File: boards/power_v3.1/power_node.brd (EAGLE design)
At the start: 80 x 51 mm, 31 parts, among them J1 AVR_SPI_PRG_6NS, J2 12146734, U1 ATtiny167, U2 MCP2025, U3 MC17XSF500

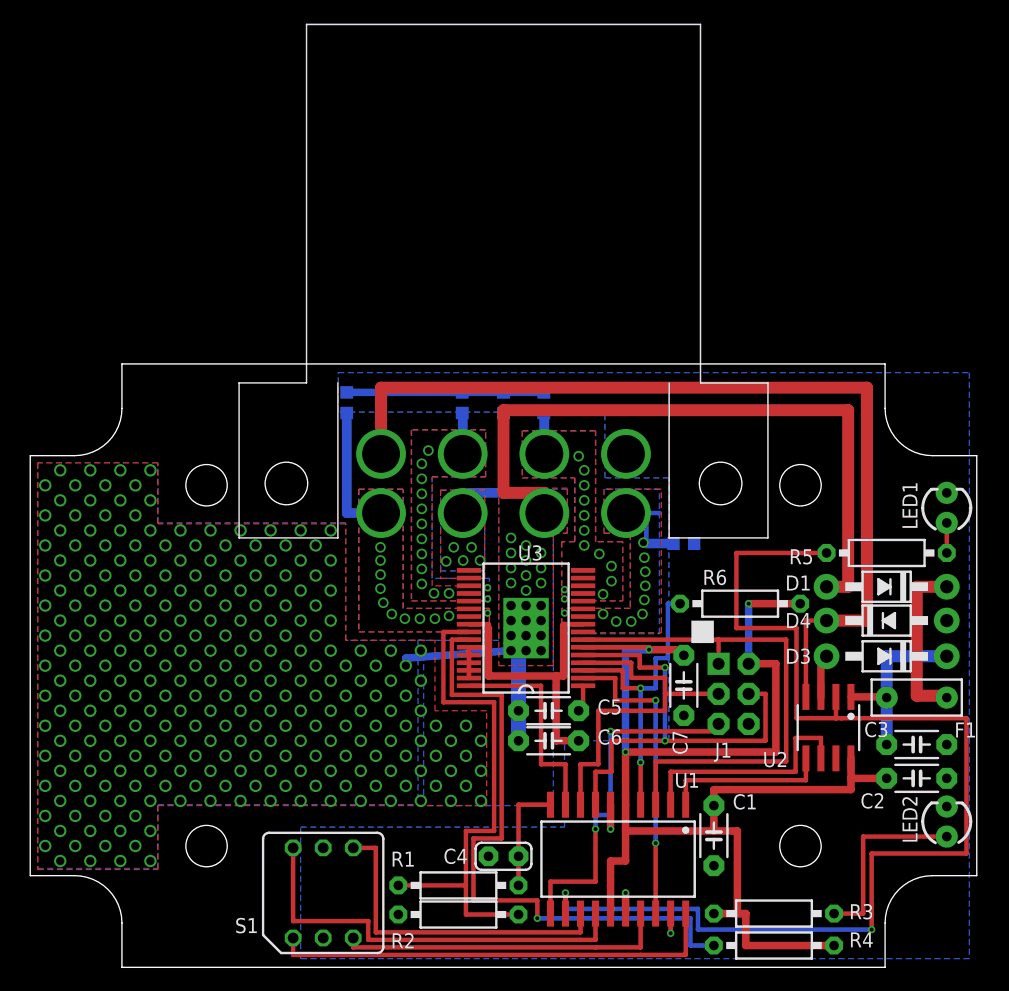
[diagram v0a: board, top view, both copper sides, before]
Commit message: Spin the power_v3 board, add more support code for it
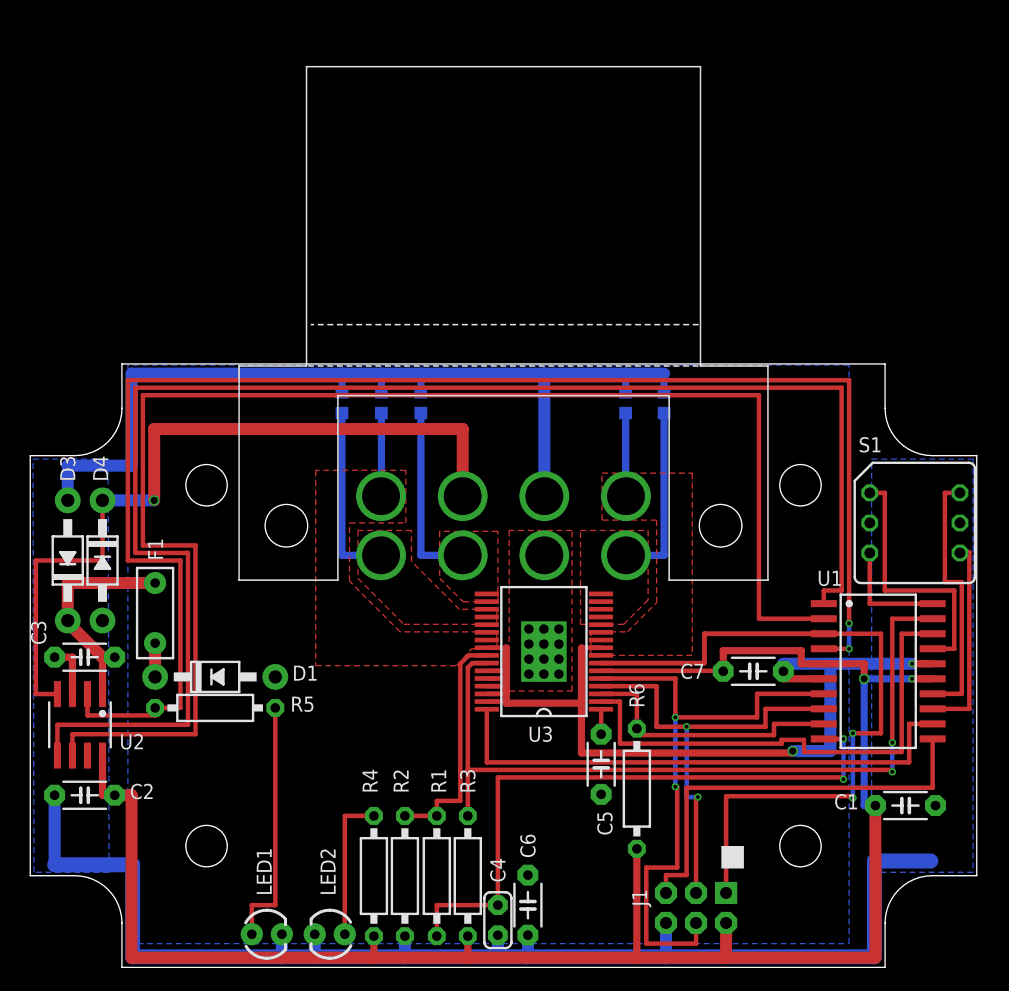
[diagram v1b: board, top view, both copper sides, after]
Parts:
- moved C3 70.7 mm to (12.2, 36.9), turned to 180 degrees
- moved C2 70.3 mm to (12.2, 25.2), turned to 180 degrees
- moved D3 69.7 mm to (10.8, 45.1), turned to 90 degrees
- moved LED1 67.8 mm to (27.6, 13.5), turned to 0 degrees
- moved D4 66.5 mm to (13.7, 45.1), turned to 270 degrees
- moved F1 64.8 mm to (18.2, 40.6), turned to 270 degrees
- moved U2 63.3 mm to (11.8, 31.2)
- moved S1 59.0 mm to (82.4, 48.3), turned to 180 degrees
- moved R5 58.2 mm to (23.3, 32.6)
- moved D1 57.3 mm to (23.3, 35.2), turned to 0 degrees
- moved LED2 53.0 mm to (32.9, 13.5), turned to 180 degrees
- moved R4 34.0 mm to (36.7, 18.4), turned to 270 degrees
- moved U1 27.1 mm to (79.3, 35.7), turned to 270 degrees
- moved R3 26.5 mm to (44.6, 18.4), turned to 270 degrees
- moved J1 18.4 mm to (63.9, 15.7), turned to 180 degrees
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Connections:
- net GND: now also J2.C; no longer J2.D
- net ID1: now also U1.17; no longer U1.20
- net ID4: now also U1.20; no longer U1.17
- net LIN: now also J2.B; no longer J2.A
- net LINCS: now also U1.4; no longer U1.12
- net OUT1: now also J2.A; no longer J2.H
- net OUT2: now also J2.D; no longer J2.E
- net OUT3: now also J2.H; no longer J2.B
- net OUT4: now also J2.E; no longer J2.C
- net SWCLK: now also U1.12; no longer U1.9
- net SWCS: now also U1.9; no longer U1.4
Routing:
- net GND: track 54.7 -> 269.6 mm
- net LINRX: track 14.1 -> 126.0 mm
- net LINTX: track 20.1 -> 121.7 mm
- net +12V: track 75.8 -> 0.00 mm, vias 278 -> 0
- net CSNS: track 9.52 -> 53.0 mm, vias 0 -> 2
- net +5V: track 117.4 -> 154.9 mm, vias 3 -> 2
- net LINCS: track 99.4 -> 128.2 mm
- net SWCLK: track 18.2 -> 45.4 mm
- net N$6: track 42.9 -> 20.1 mm
- net N$3: track 2.54 -> 21.1 mm
- net ID4: track 27.9 -> 9.60 mm
- net MISO: track 44.2 -> 61.5 mm, vias 0 -> 2
- net SWRSTB: track 26.0 -> 42.9 mm, vias 2 -> 0
- net ID1: track 38.1 -> 22.1 mm
- net ID8: track 35.6 -> 22.1 mm
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- removed copper zone on layer 16, net OUT1
- removed copper zone on layer 16, net OUT2
- removed copper zone on layer 16, net OUT3
- removed copper zone on layer 16, net OUT4
- removed copper zone on layer 16, net OUT5
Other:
- board text added: "LIN power node v3.1 (c)2014 michael smith"
- board text removed: "LIN power node v3 (c)2014 michael smith"
